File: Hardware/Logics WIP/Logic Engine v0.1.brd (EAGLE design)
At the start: 61 x 25.4 mm, 32 parts, among them IC1 MEGA328P, Y1 16MHz

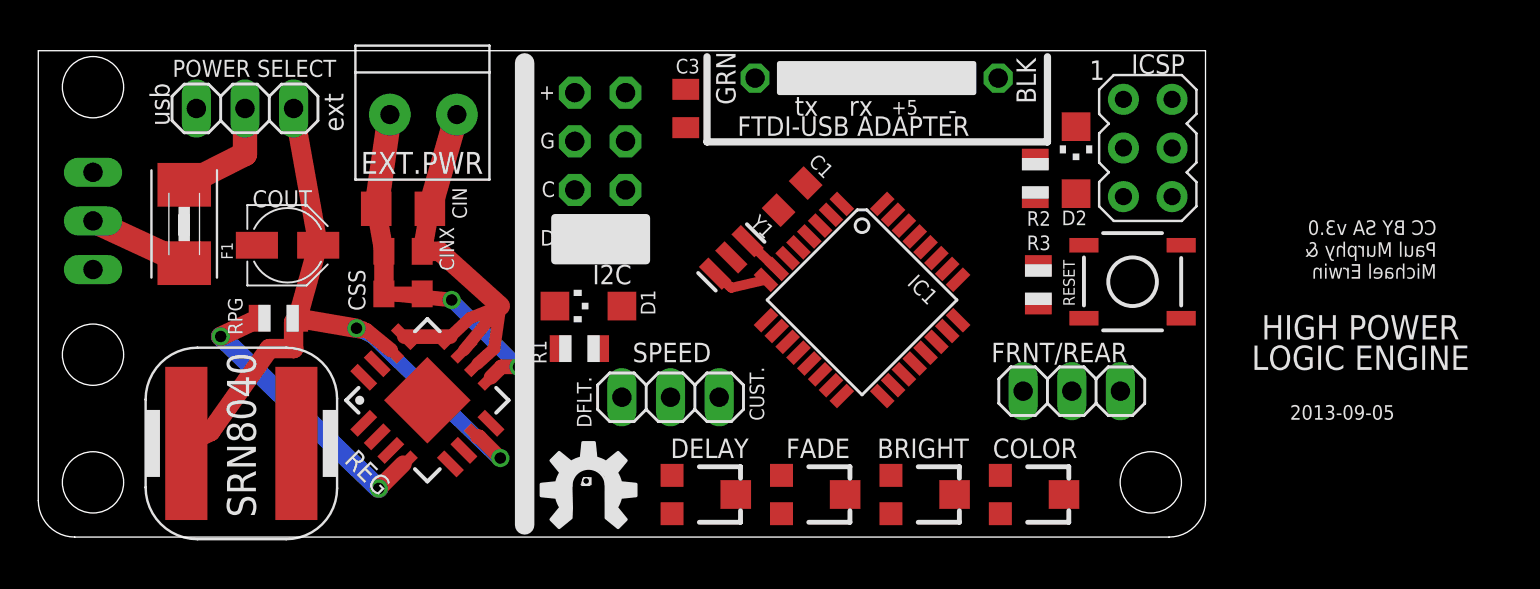
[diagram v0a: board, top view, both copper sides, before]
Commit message: 
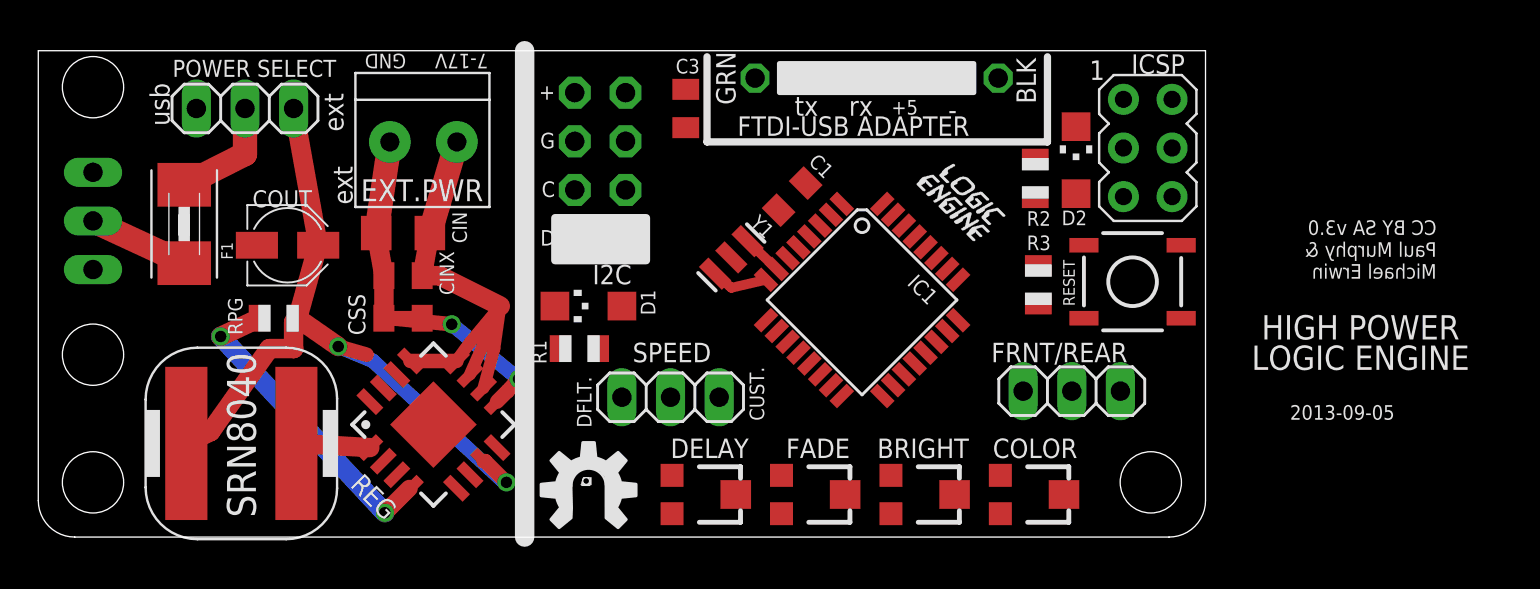
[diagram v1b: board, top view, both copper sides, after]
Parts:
- moved EXT.PWR 1.43 mm to (20.2, 20.6)
- moved REG 1.31 mm to (20.6, 5.87)
- moved CIN 1.27 mm to (19.1, 15.9)
- moved CINX 1.27 mm to (19.1, 13.7)
- moved CSS 1.27 mm to (19.1, 11.4)
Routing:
- net N$3: track 0.00 -> 3.84 mm
- net N$6: track 24.5 -> 26.0 mm
- net N$8: track 15.5 -> 16.6 mm
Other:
- board text added: "7-17V"
- board text added: "GND"

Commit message: 
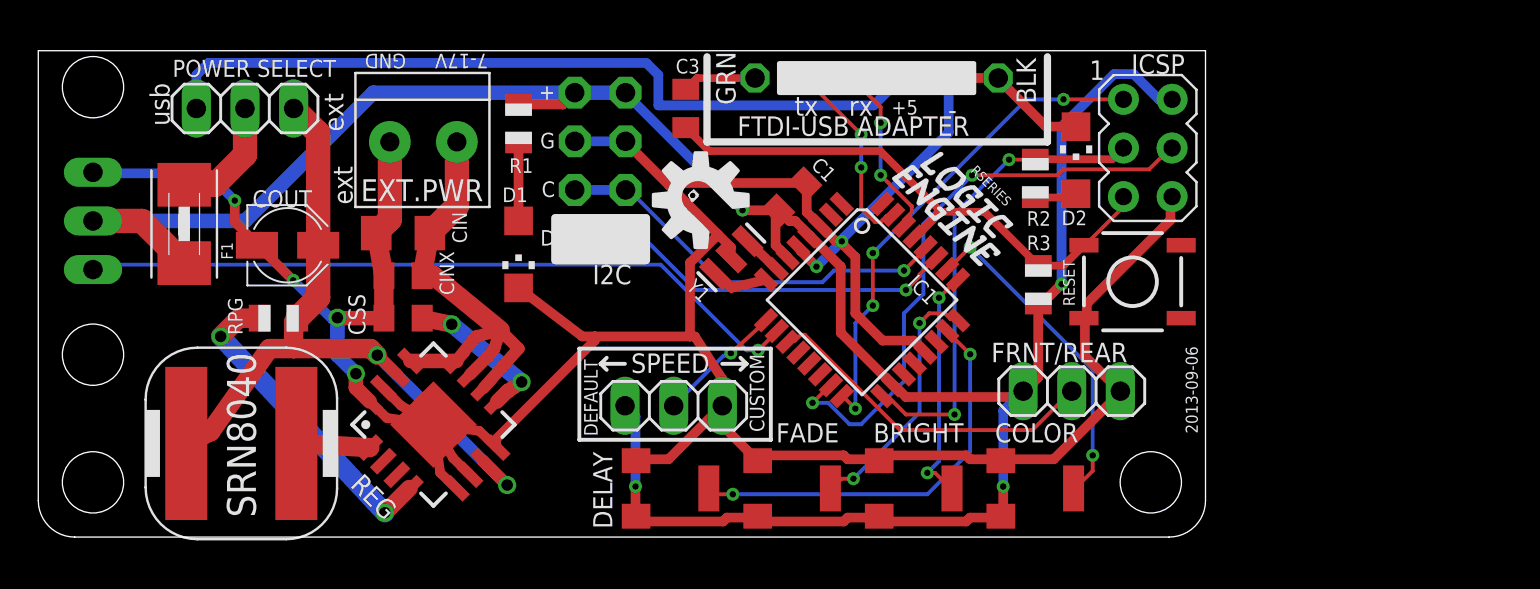
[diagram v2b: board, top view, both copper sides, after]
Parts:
- BRIGHT, COLOR, DELAY, FADE: device adafruit:TC33X -> rseries:3364
- moved U$2 16.1 mm to (34.5, 17.6), turned to 45 degrees
- moved R1 12.2 mm to (25.1, 21.6), turned to 90 degrees
- moved D1 4.54 mm to (25.1, 14.8), turned to 180 degrees
- moved DELAY 1.93 mm to (33.0, 2.54)
- moved FADE 1.31 mm to (39.4, 2.54)
- moved BRIGHT 0.71 mm to (45.7, 2.54)
- moved SPEED 0.47 mm to (33.2, 6.86)
- moved COLOR 0.32 mm to (52.1, 2.54)
- turned C1 to 45 degrees
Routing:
- net GND: track 9.30 -> 175.4 mm, vias 0 -> 6
- net +5V: track 5.25 -> 127.1 mm, vias 0 -> 4
- net USB_5V: track 0.00 -> 41.2 mm
- net DIGITAL6: track 0.00 -> 38.1 mm, vias 0 -> 1
- net RST: track 0.00 -> 31.5 mm
- net MOSI: track 0.00 -> 30.8 mm, vias 0 -> 2
- net MISO: track 0.00 -> 25.9 mm, vias 0 -> 4
- net SCK: track 0.00 -> 24.9 mm, vias 0 -> 2
- net ANALOG0: track 0.00 -> 21.5 mm, vias 0 -> 2
- net ANALOG5: track 0.00 -> 21.1 mm, vias 0 -> 1
- net ANALOG4: track 0.00 -> 20.7 mm, vias 0 -> 1
- net DIGITAL7: track 0.00 -> 17.9 mm
- net ANALOG3: track 0.00 -> 17.4 mm, vias 0 -> 2
- net ANALOG1: track 0.00 -> 13.3 mm, vias 0 -> 2
- net ANALOG2: track 0.00 -> 12.4 mm, vias 0 -> 2
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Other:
- board text added: "2013-09-06"
- board text added: "CUSTOM"
- board text added: "DEFAULT"
- board text added: "RSERIES"
- board text removed: "2013-09-05"
- board text removed: "CC BY SA v3.0 Paul Murphy & Michael Erwin"
- board text removed: "CUST."
- board text removed: "DFLT."
- board text removed: "HIGH POWER LOGIC ENGINE"

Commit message: 
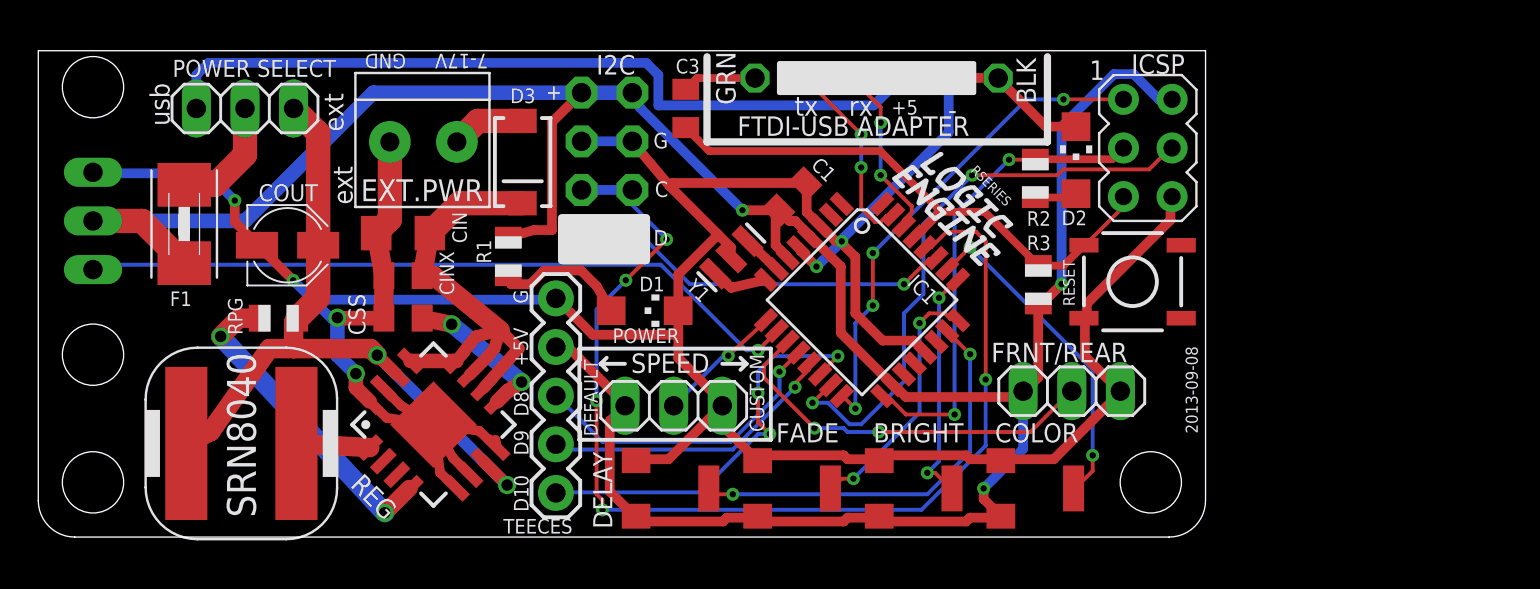
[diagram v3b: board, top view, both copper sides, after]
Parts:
- removed U$2: RSERIES-OSHW-LOGOMEDIUM, rseries:RSERIES-OSHW-LOGO-MEDIUM
- added D3: BA340LA, SparkFun-DiscreteSemi:SMA-DIODE
- added TEECES: (no value), SparkFun-Connectors:1X05
- moved D1 7.21 mm to (31.7, 11.8), turned to 270 degrees
- moved R1 6.95 mm to (24.5, 14.7)
- moved I2C 0.36 mm to (28.4, 19.4)
- moved I2C1 0.36 mm to (31.0, 19.4)
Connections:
- new net N$11: D3.A, EXT.PWR.2
- net +5V: now also TEECES.2
- net DIGITAL10: now also TEECES.5
- net DIGITAL8: now also TEECES.3
- net DIGITAL9: now also TEECES.4
- net GND: now also TEECES.1
- net N$6: now also D3.C; no longer EXT.PWR.2
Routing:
- net ANALOG5: track 21.1 -> 58.1 mm, vias 1 -> 5
- net DIGITAL10: track 0.00 -> 21.8 mm, vias 0 -> 3
- net DIGITAL8: track 0.00 -> 16.2 mm, vias 0 -> 1
- net DIGITAL9: track 0.00 -> 15.5 mm, vias 0 -> 1
- net +5V: track 127.1 -> 140.9 mm, vias 4 -> 3
- net N$11: track 0.00 -> 3.89 mm
- net N$5: track 4.08 -> 7.06 mm
- net GND: track 175.4 -> 178.3 mm
- net DIGITAL7: track 17.9 -> 20.5 mm, vias 0 -> 2
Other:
- board text added: "+5V"
- board text added: "2013-09-08"
- board text added: "D10"
- board text added: "D8"
- board text added: "D9"
- board text added: "POWER"
- board text removed: "2013-09-06"

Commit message: 
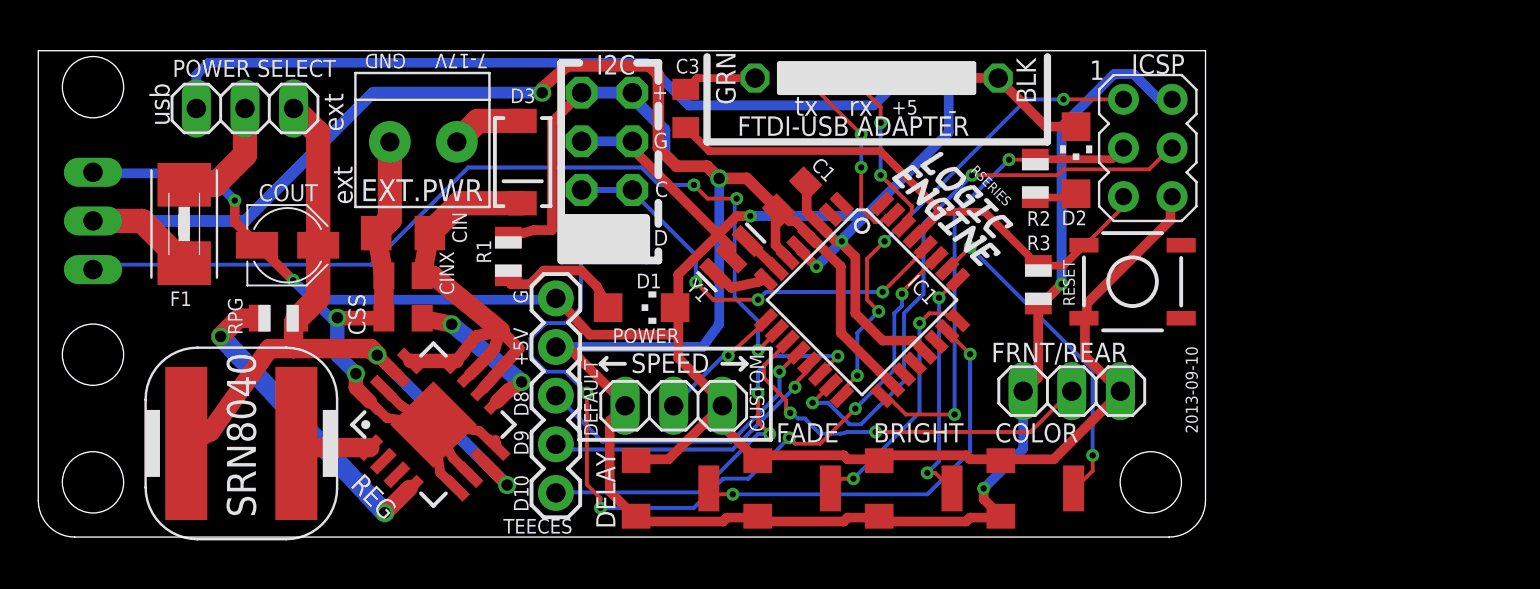
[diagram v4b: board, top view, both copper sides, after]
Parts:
- moved D1 0.22 mm to (31.5, 12.0)
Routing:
- net ANALOG5: track 58.1 -> 22.4 mm, vias 5 -> 3
- net ANALOG4: track 20.7 -> 45.9 mm, vias 1 -> 5
- net +5V: track 140.9 -> 163.4 mm, vias 3 -> 4
- net DIGITAL6: track 38.1 -> 46.4 mm, vias 1 -> 3
- net GND: track 178.3 -> 179.6 mm, vias 6 -> 7
- net USB_5V: track 41.2 -> 40.3 mm
- net MISO: track 25.9 -> 25.1 mm
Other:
- board text added: "2013-09-10"
- board text removed: "2013-09-08"
